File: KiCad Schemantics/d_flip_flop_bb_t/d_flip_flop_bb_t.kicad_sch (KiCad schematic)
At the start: 10 parts

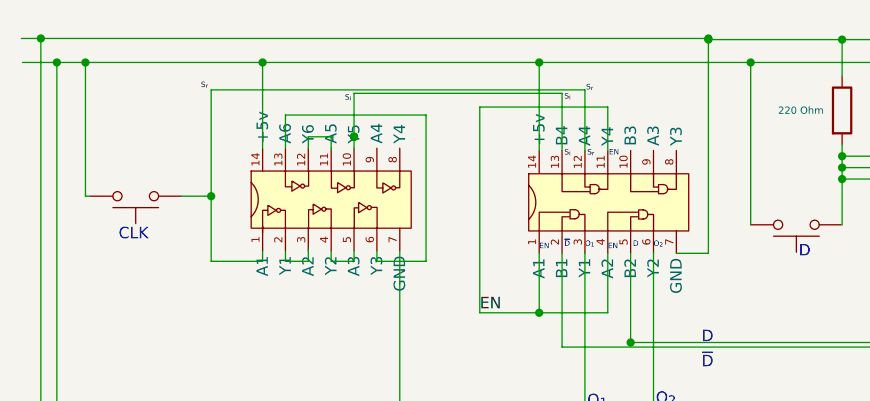
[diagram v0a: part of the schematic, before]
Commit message: Fixed the D Flip Flop
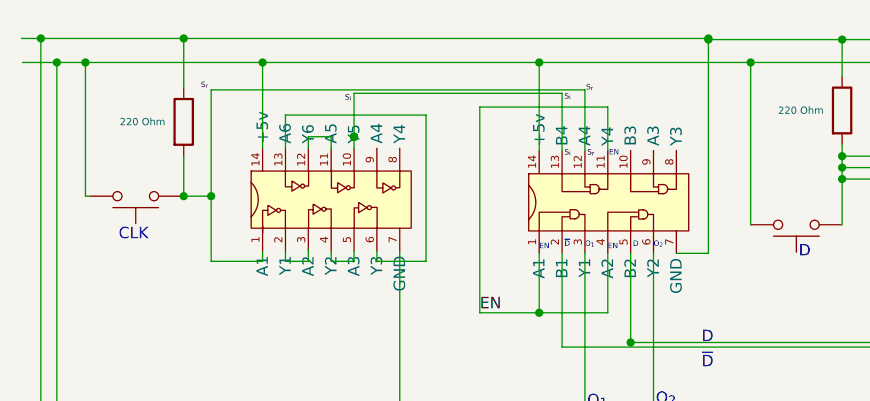
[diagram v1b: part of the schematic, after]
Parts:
- added R?: 220 Ohm, symbol Device:R
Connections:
- net -: now also R?.1
- net at SW?.1: now also R?.2
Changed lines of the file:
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@@
   (junction (at 109.22 62.865) (diameter 0) (color 0 0 0 0)
   )
+  (junction (at 100.457 60.198) (diameter 0) (color 0 0 0 0)
+  )
   (junction (at 173.609 74.549) (diameter 0) (color 0 0 0 0)
   )
@@
   (junction (at 119.3801 71.12) (diameter 0) (color 0 0 0 0)
   )
+  (junction (at 100.457 77.724) (diameter 0) (color 0 0 0 0)
+  )
   (junction (at 158.75 60.325) (diameter 0) (color 0 0 0 0)
   )
@@
     (stroke (width 0) (type default) (color 0 0 0 0))
   )
+  (wire (pts (xy 100.457 73.279) (xy 100.457 77.724))
+    (stroke (width 0) (type default) (color 0 0 0 0))
+  )
   (wire (pts (xy 173.609 73.279) (xy 173.609 74.549))
     (stroke (width 0) (type default) (color 0 0 0 0))
@@
     (stroke (width 0) (type default) (color 0 0 0 0))
   )
+  (wire (pts (xy 100.457 60.198) (xy 158.75 60.198))
+    (stroke (width 0) (type default) (color 0 0 0 0))
+  )
   (wire (pts (xy 182.753 130.302) (xy 190.373 130.302))
     (stroke (width 0) (type default) (color 0 0 0 0))
@@
     (stroke (width 0) (type default) (color 0 0 0 0))
   )
-  (wire (pts (xy 100.203 77.724) (xy 103.505 77.724))
+  (wire (pts (xy 100.203 77.724) (xy 100.457 77.724))
     (stroke (width 0) (type default) (color 0 0 0 0))
   )
@@
     (stroke (width 0) (type default) (color 0 0 0 0))
   )
-  (wire (pts (xy 84.582 60.198) (xy 158.75 60.198))
+  (wire (pts (xy 84.582 60.198) (xy 100.457 60.198))
     (stroke (width 0) (type default) (color 0 0 0 0))
   )
@@
     (stroke (width 0) (type default) (color 0 0 0 0))
   )
+  (wire (pts (xy 100.457 77.724) (xy 103.505 77.724))
+    (stroke (width 0) (type default) (color 0 0 0 0))
+  )
   (wire (pts (xy 145.034 83.947) (xy 145.034 103.632))
+    (stroke (width 0) (type default) (color 0 0 0 0))
+  )
+  (wire (pts (xy 100.457 60.198) (xy 100.457 65.659))
     (stroke (width 0) (type default) (color 0 0 0 0))
   )
@@
     (pin "2")
   )
+  (symbol (lib_id "Device:R") (at 100.457 69.469 0) (unit 1)
+    (in_bom yes) (on_board yes)
+    (property "Reference" "R?" (id 0) (at 102.997 68.1989 0)
+      (effects (font (size 1.27 1.27)) (justify left) hide)
+    )
+    (property "Value" "220 Ohm" (id 1) (at 93.345 69.469 0)
+      (effects (font (size 0.8 0.8)) (justify left))
+    )
+    (property "Footprint" "" (id 2) (at 98.679 69.469 90)
+      (effects (font (size 1.27 1.27)) hide)
+    )
+    (property "Datasheet" "~" (id 3) (at 100.457 69.469 0)
+      (effects (font (size 1.27 1.27)) hide)
+    )
+    (pin "1")
+    (pin "2")
+  )
   (symbol (lib_id "Device:R") (at 190.373 117.983 0) (unit 1)
     (in_bom yes) (on_board yes)
@@
       (reference "R?") (unit 1) (value "220 Ohm") (footprint "")
     )
+    (path "/76c0a953-db3d-4929-907f-1ee2da36860d"
+      (reference "R?") (unit 1) (value "220 Ohm") (footprint "")
+    )
